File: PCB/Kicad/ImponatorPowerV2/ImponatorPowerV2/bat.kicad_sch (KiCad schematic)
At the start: 8 parts, among them U6 MCP73831T-2ACI/OT

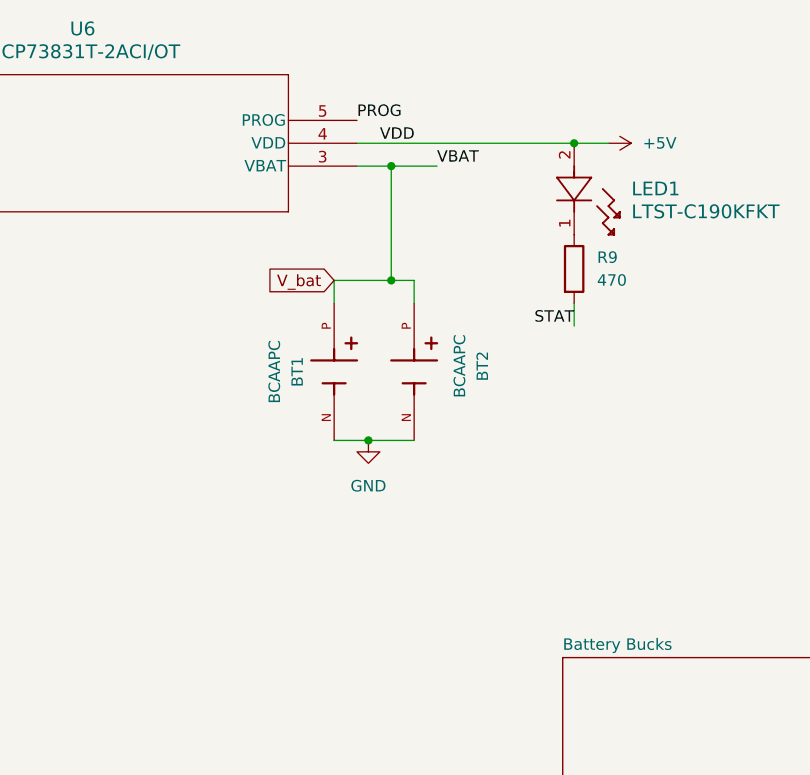
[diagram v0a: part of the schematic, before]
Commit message: PCB routed, not ready for production
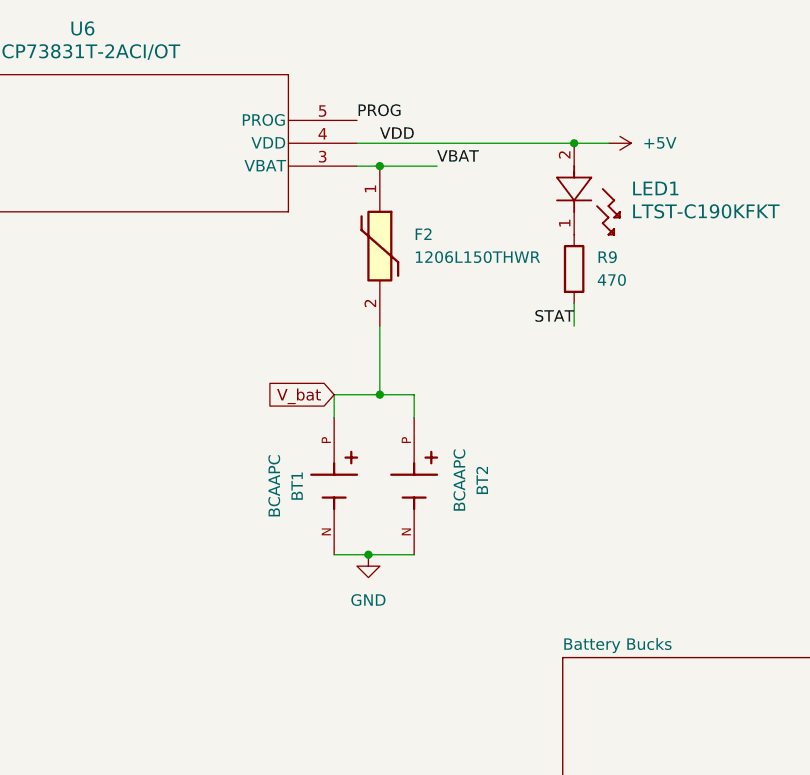
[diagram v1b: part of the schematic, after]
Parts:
- added F2: 1206L150THWR, custom2:FUSC3216X100N, symbol imported2:1206L150THWR
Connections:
- net V_bat: now also F2.2; no longer C7.2, U6.3 (VBAT)
- new net VBAT: C7.2, F2.1, U6.3 (VBAT)
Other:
- moved on the sheet: BT1, BT2
